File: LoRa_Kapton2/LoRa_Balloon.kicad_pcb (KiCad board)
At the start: 2 copper layers, 30 x 56 mm, 248 parts, among them J1 COAX, J2 Qwicc_6-pin, U1 SKY67013-396LF_CID141, U2 SX1272IMLTRICT-ND_CID104, U3 SKY67013-396LF_CID141, U4 PE4259_CID105, U5 ATMEGA328P-AU, X1 X1E0000210162_CID142, X2 7A-12.000MAAJ-T_CID117

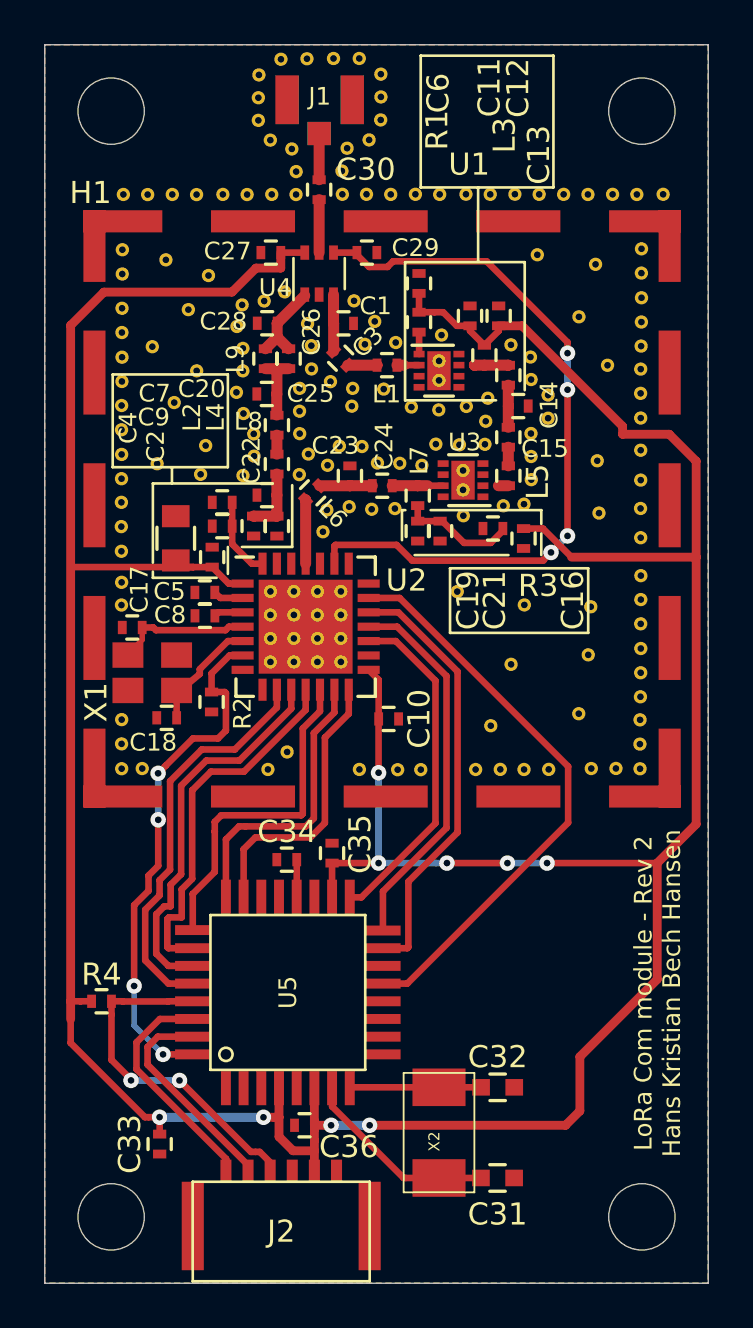
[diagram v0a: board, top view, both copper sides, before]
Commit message: New folder structure - more versions
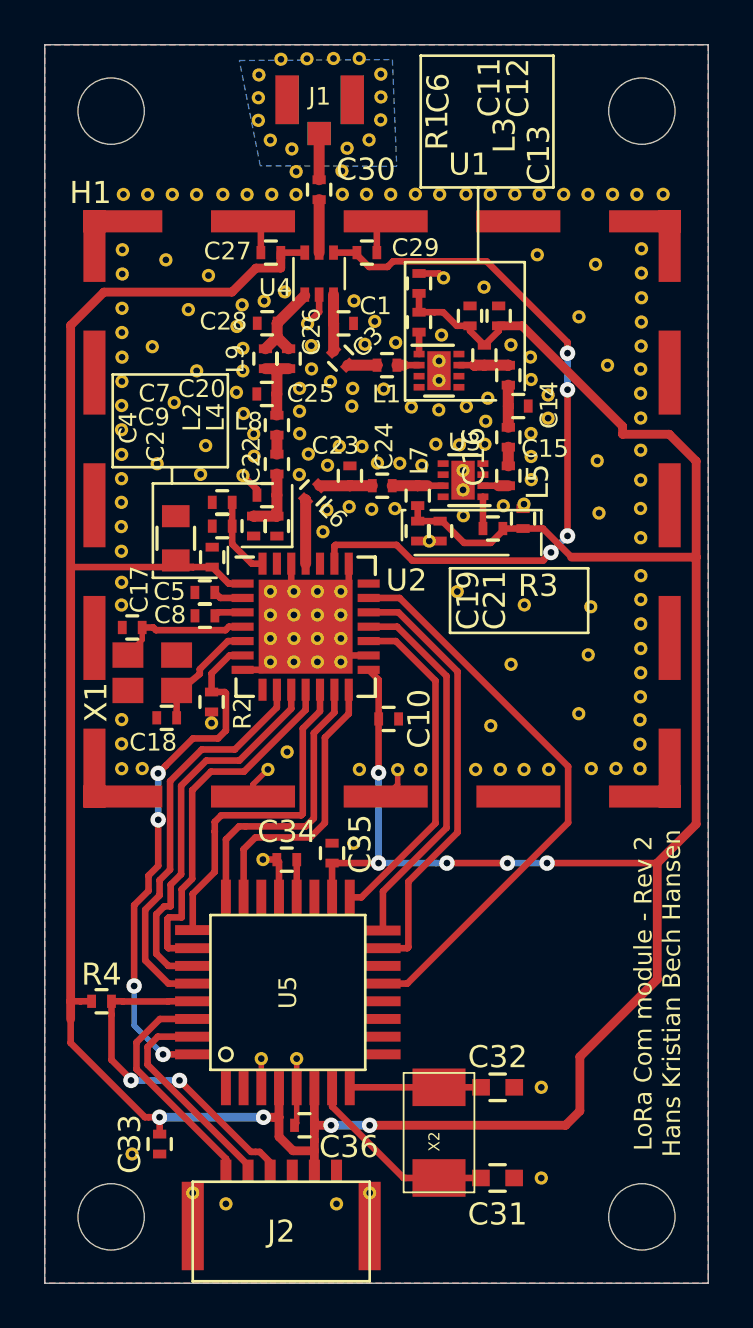
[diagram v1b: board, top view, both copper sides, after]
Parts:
- added ?: , dtusat:via-0.6mm-0.3mm_drill, F.Cu at (203.2, 125.3)
- added ?: , dtusat:via-0.6mm-0.3mm_drill, F.Cu at (192.5, 154.8)
- added ?: , dtusat:via-0.6mm-0.3mm_drill, F.Cu at (189.7, 153.0)
- added ?: , dtusat:via-0.6mm-0.3mm_drill, F.Cu at (208.2, 154.1)
- added ?: , dtusat:via-0.6mm-0.3mm_drill, F.Cu at (208.2, 150.0)
- added ?: , dtusat:via-0.6mm-0.3mm_drill, F.Cu at (195.6, 148.7)
- added ?: , dtusat:via-0.6mm-0.3mm_drill, F.Cu at (197.2, 148.7)
- added ?: , dtusat:via-0.6mm-0.3mm_drill, F.Cu at (199.8, 139.0)
- added ?: , dtusat:via-0.6mm-0.3mm_drill, F.Cu at (195.7, 139.7)
- added ?: , dtusat:via-0.6mm-0.3mm_drill, F.Cu at (203.8, 113.4)
- added ?: , dtusat:via-0.6mm-0.3mm_drill, F.Cu at (205.7, 113.8)
- added ?: , dtusat:via-0.6mm-0.3mm_drill, F.Cu at (193.3, 133.5)
- added ?: , dtusat:via-0.6mm-0.3mm_drill, F.Cu at (194.0, 155.3)
- added ?: , dtusat:via-0.6mm-0.3mm_drill, F.Cu at (199.0, 155.3)
- added ?: , dtusat:via-0.6mm-0.3mm_drill, F.Cu at (200.5, 154.8)
- moved C16 0.90 mm to (207.4, 124.3), turned to 90 degrees
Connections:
- C10 pad 1: +3V3 -> Net-(C10-Pad1)
- C2 pad 1: +3V3 -> Net-(C10-Pad1)
- J1 pad 3: (no net) -> GND
- J1 pad 4: (no net) -> GND
- R2 pad 2: /RXTX_SW -> /Reset_SX
- U2 pad 1: +3V3 -> Net-(C10-Pad1)
- U2 pad 15: +3V3 -> Net-(C10-Pad1)
- U2 pad 6: /RXTX_SW -> /Reset_SX
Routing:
- net GND: track 0.00 -> 24.1 mm
- net Net-(R3-Pad2): track 0.00 -> 1.44 mm
- net Net-(C13-Pad2): track 1.54 -> 2.69 mm
- net Net-(L5-Pad1): track 0.45 -> 1.60 mm
- net +3V3: track 174.2 -> 175.2 mm
